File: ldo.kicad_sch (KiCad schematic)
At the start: 9 parts, among them U1 MIC5504-3.3YM5

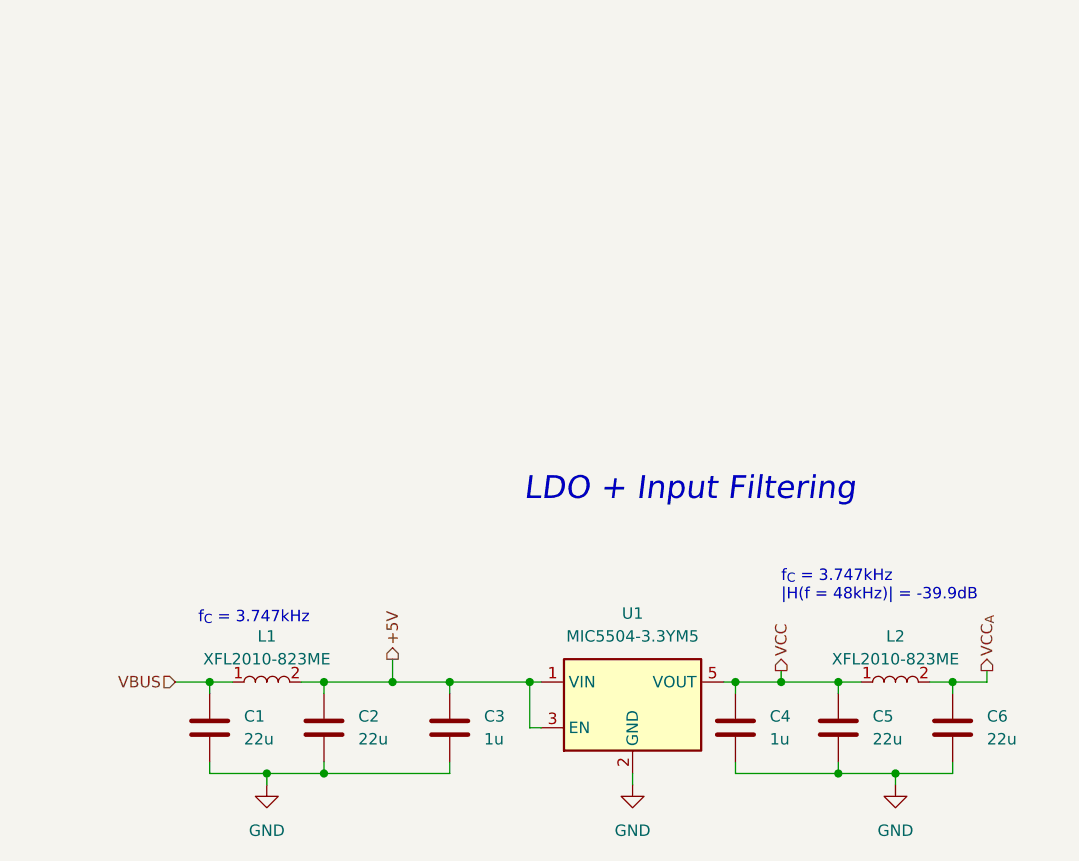
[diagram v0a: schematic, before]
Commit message: Redid schematic and component values according to new recalculations
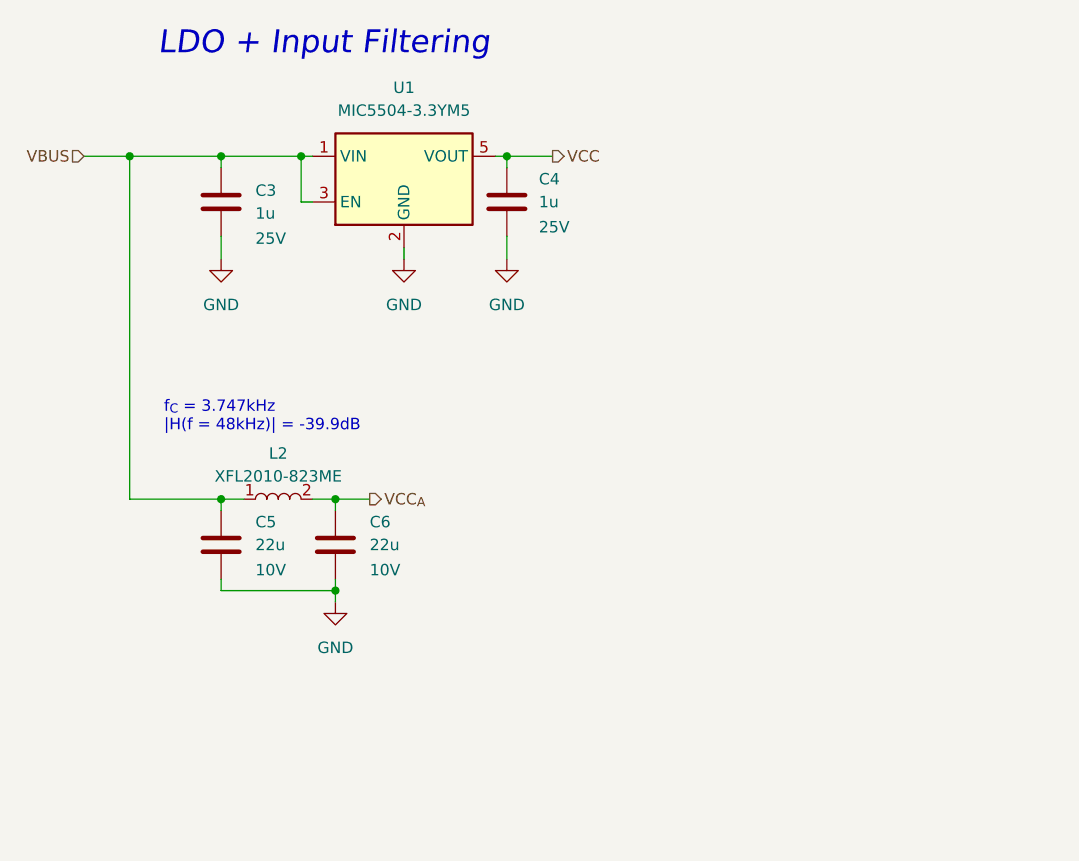
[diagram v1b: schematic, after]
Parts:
- removed C1, C2: 22u, Capacitor_SMD:C_1210_3225Metric_Pad1.33x2.70mm_HandSolder, symbol Device:C
- removed L1: XFL2010-823ME, Inductor_SMD:L_Coilcraft_XFL2010, symbol Device:L
- C3, C4: footprint Capacitor_SMD:C_1206_3216Metric_Pad1.33x1.80mm_HandSolder -> Capacitor_SMD:C_0603_1608Metric_Pad1.08x0.95mm_HandSolder; Mouser Part Number 581-TAJA105K020TNJ -> 187-CL10B105KA8NNNL; Voltage Rating (none) -> 25V
- C5, C6: footprint Capacitor_SMD:C_1210_3225Metric_Pad1.33x2.70mm_HandSolder -> Capacitor_SMD:C_0805_2012Metric_Pad1.18x1.45mm_HandSolder; Mouser Part Number 80-C1210C226K8R -> 187-CL21A226MPQNNNE; Voltage Rating (none) -> 10V
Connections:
- net +5V is gone; now on net VBUS: C3.1, U1.1 (VIN), U1.3 (EN)
- net VBUS: now also C5.1, L2.1
- net VCC: no longer C5.1, L2.1
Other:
- note removed: "f_{C} = 3.747kHz"
- moved on the sheet: C3, C4, C5, C6, L2, U1
